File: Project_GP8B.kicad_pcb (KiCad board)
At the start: 4 copper layers, 133 x 93 mm, 103 parts, among them IC1 XC2C256-VQ100, J1 ALU_JTAG, J2 TE_Eurocard_96pole, J3 MM1_5530843-2, J4 UnusedPins_Connector, J5 ALU_PINS, U1 74AHC05, U10 74AHC1G04, U11 CD74AC238, U12 74AHC1G04, U13 CD74AC238, U14 74AHC08, U15 CD74AC238, U16 74AHC08, U17 74AHC138, U18 74HC165, U19 74AHCT244, U2 74AHC05, U20 74AHCT244, U21 74AHCT244, U22 74AHCT244, U23 74AHCT244, U24 74AHC273, U25 74AHCT595, U26 74AHC273, U27 74AHC273, U28 TPS7A0518PDBZR, U29 74AHC273, U3 74AHC1G04, U30 SN74LVC8T245DW, U31 74AHC273, U32 SN74AVC4T245D, U33 74AHC273, U34 74LVC1G34, U35 74AHC273, U36 74AHC1G04, U37 74AHC273, U38 74AHC374, U39 74AHC1G04, U4 74AHC1G04, U5 74AHC05, U6 74AHC273, U7 74AHCT273, U8 74HC163, U9 CD74AC238

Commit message: Apply date (19.08.2020), QRcode fix
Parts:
- added G***: LOGO, QRCode:QRCode, B.Cu at (157.3, 80.8)

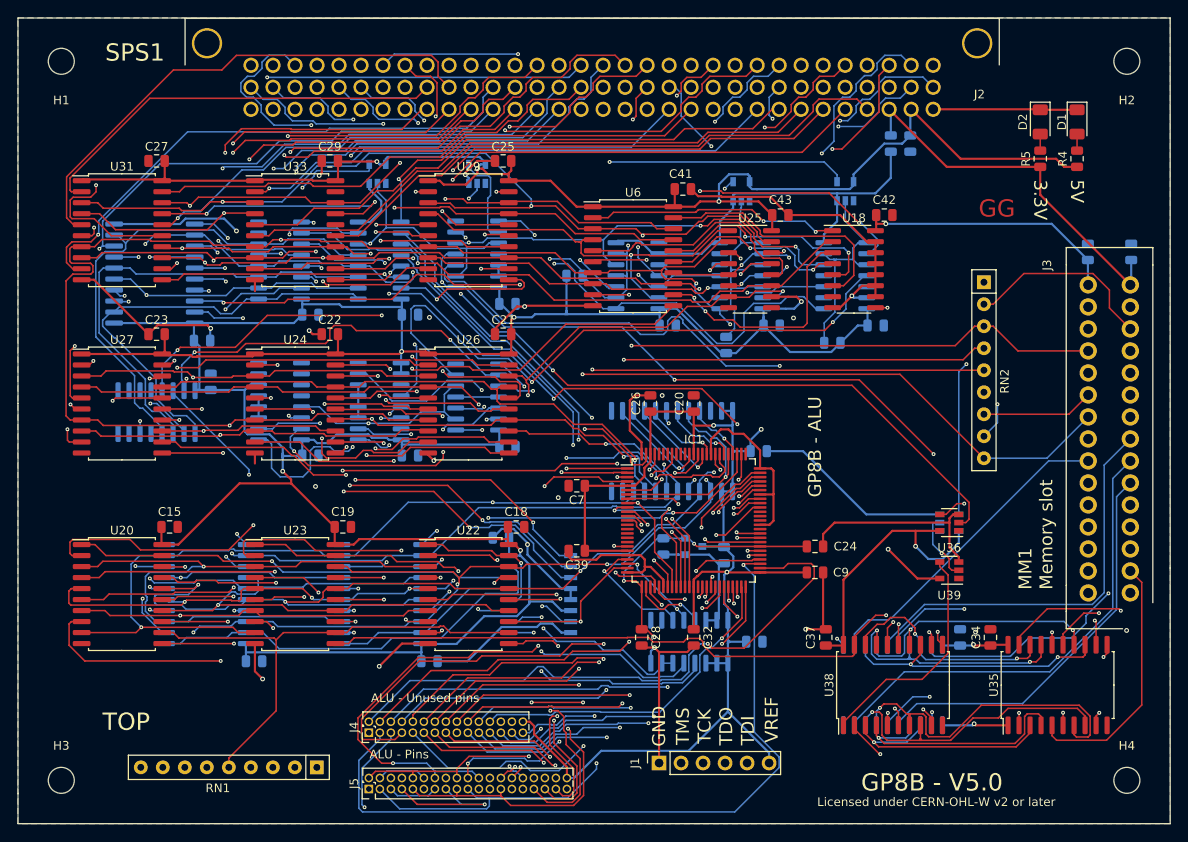
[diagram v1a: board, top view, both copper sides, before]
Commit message: V5.1 (#9)
* Apply new symbol for XC2C256-VQ100 #5

* Set new date and 5.1

* Replacing 74HC165 with 74HC166, and add SPI_CFG_DS #4

* Replace some gates with a 74AHC1G02 to fix the pulse problem #3

* Go next only if SRCVALUE, (simple instruction)

* Remove weird ghost bus in register

* Small cleaning in fileRegister

* Go next only if SRCVALUE, (complex instruction) #8
adding 74AHC1G08

* Better decoupling #6

* Component association (#7)

* netlist

* Updated BOM for V5.1

* Routing, cleaning first pass

* bit of pcb cleaning

* SolderMaskClearance to 0

* Schematics to pdf

* PCB files in pdf

* exporting Gerbert files

* new 3d images

* Update README.md

* Modifying CHANGELOG file

* Update README.md
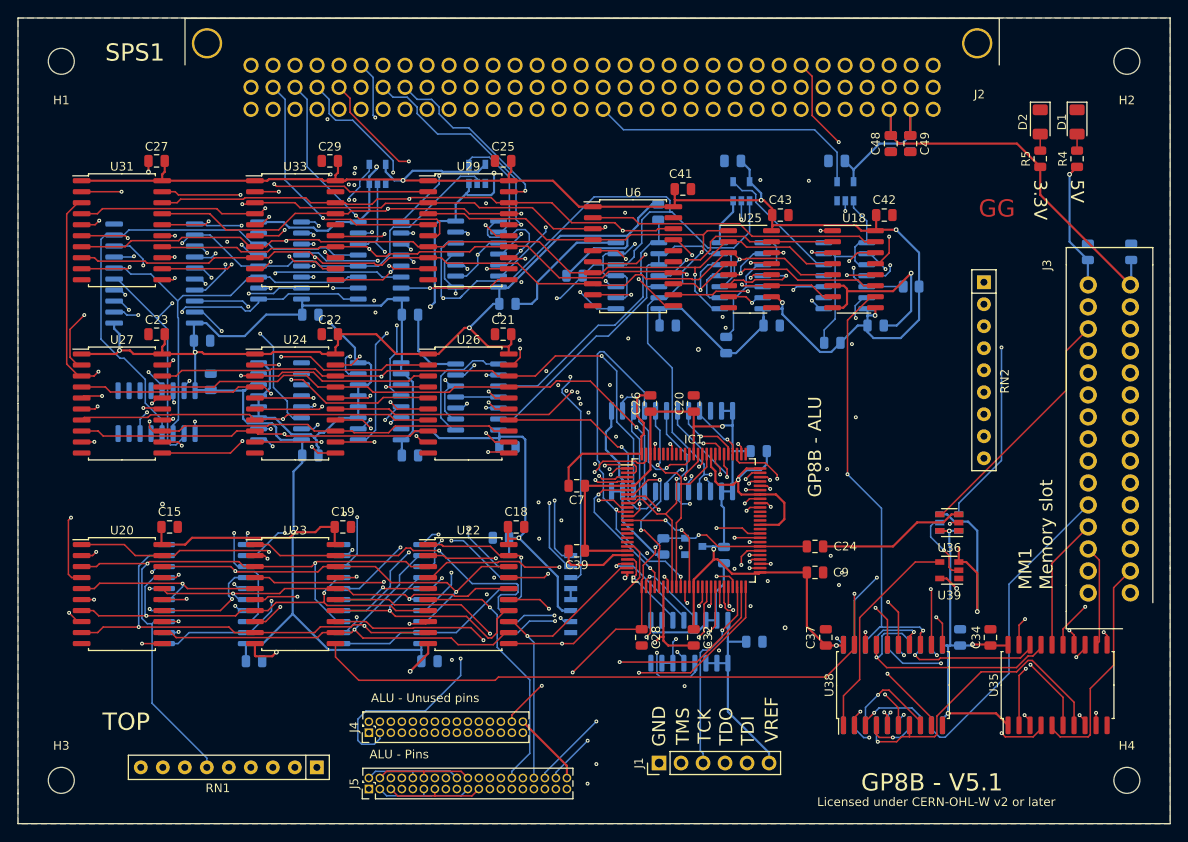
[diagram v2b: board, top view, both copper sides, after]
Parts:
- added C46: 10nF, Capacitor_SMD:C_0805_2012Metric, B.Cu at (155.5, 48.0)
- added C47: 10nF, Capacitor_SMD:C_0805_2012Metric, B.Cu at (143.5, 48.0)
- added C48: 1uF, Capacitor_SMD:C_0805_2012Metric, F.Cu at (161.8, 46.0)
- added C49: 1uF, Capacitor_SMD:C_0805_2012Metric, F.Cu at (164.0, 46.0)
- added R6: 10k, Resistor_SMD:R_0805_2012Metric, B.Cu at (134.9, 53.9)
- added R7: 10k, Resistor_SMD:R_0805_2012Metric, B.Cu at (164.1, 62.5)
- C30, C31, C36, C38: value 10nF -> 100nF
- J1: footprint Connector_PinSocket_2.54mm:PinSocket_1x06_P2.54mm_Vertical -> Connector_PinHeader_2.54mm:PinHeader_1x06_P2.54mm_Vertical
- U18: value 74HC165 -> 74HC166
- U3: value 74AHC1G04 -> 74AHC1G02
- U4: value 74AHC1G04 -> 74AHC1G08
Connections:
- R3 pad 2: /~ADDSRC_CLK -> /~NEXT_CLK
- U1 pad 8: Net-(U1-Pad8) -> /IF_RESULT
- U1 pad 9: GND -> /~IF_RESULT
- U14 pad 11: Net-(U14-Pad11) -> /NEXT_ISIMPLE
- U14 pad 12: GND -> /END_ISIMPLE
- U14 pad 13: GND -> /SELECTING_SRC
- U17 pad 15: /NumberSelect/~SELECTING_SRC -> /~SELECTING_SRC
- U18 pad 1: /SPI/SPI_CFG_~PL -> /SPI/SPI_CFG_DS
- U18 pad 10: GND -> /NUMBER_4
- U18 pad 11: GND -> /NUMBER_5
- U18 pad 12: GND -> /NUMBER_6
- U18 pad 13: GND -> /SPI_MOSI
- U18 pad 14: GND -> /NUMBER_7
- U18 pad 15: GND -> /SPI/SPI_CFG_~PL
- U18 pad 2: /SPI_CLK -> /NUMBER_0
- U18 pad 3: /SPI/BUFF_0 -> /NUMBER_1
- U18 pad 4: /SPI/BUFF_1 -> /NUMBER_2
- U18 pad 5: /SPI/BUFF_2 -> /NUMBER_3
- U18 pad 6: /SPI/BUFF_3 -> GND
- U18 pad 7: Net-(U18-Pad7) -> /SPI_CLK
- U18 pad 9: /SPI_MOSI -> +5V
- U19 pad 1: /NumberSelect/~SELECTING_SRC -> /~SELECTING_SRC
- U19 pad 19: /NumberSelect/~SELECTING_SRC -> /~SELECTING_SRC
- U3 pad 1: (no net) -> /~NEXT_CLK
- U3 pad 2: /~ADDSRC_CLK -> /GLOBAL_CLK
- U4 pad 1: (no net) -> /END_MAXCOUNT
- U4 pad 2: /~IF_RESULT -> /SELECTING_SRC
- U4 pad 4: /IF_RESULT -> /NEXT_MAXCOUNT
- U5 pad 1: /END_ISIMPLE -> /NEXT_ISIMPLE
- U5 pad 10: /~ADDSRC_CLK -> /~NEXT_CLK
- U5 pad 12: Net-(U5-Pad12) -> /SELECTING_SRC
- U5 pad 13: GND -> /~SELECTING_SRC
- U5 pad 2: /~ADDSRC_CLK -> /~NEXT_CLK
- U5 pad 4: /~ADDSRC_CLK -> /~NEXT_CLK
- U5 pad 5: /END_MAXCOUNT -> /NEXT_MAXCOUNT
- U5 pad 6: /~ADDSRC_CLK -> /~NEXT_CLK
- U5 pad 8: /~ADDSRC_CLK -> /~NEXT_CLK
- U6 pad 12: /SPI/BUFF_0 -> /SPI_CS
- U6 pad 15: /SPI/BUFF_1 -> Net-(U6-Pad15)
- U6 pad 16: /SPI/BUFF_2 -> Net-(U6-Pad16)
- U6 pad 19: /SPI/BUFF_3 -> Net-(U6-Pad19)
- U6 pad 6: /SPI_SCLK -> /SPI/SPI_CFG_DS
- U6 pad 9: /SPI_CS -> /SPI_SCLK
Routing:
- net /~SELECTING_SRC: track 0.00 -> 108.1 mm, vias 0 -> 3
- net GND: track 420.0 -> 338.7 mm, vias 20 -> 17
- net /BRAMADD1_CLK: track 184.9 -> 120.4 mm, vias 2 -> 3
- net /SELECTING_SRC: track 0.00 -> 56.4 mm, vias 0 -> 3
- net /Connector/BREAD1_7: track 99.3 -> 147.9 mm
- net /NumberSelect/~SELECTING_SRC: track 48.3 -> 0.00 mm
- net /NUMBER_1: track 434.3 -> 391.3 mm, vias 8 -> 10
- net /NEXT_ISIMPLE: track 0.00 -> 42.2 mm, vias 0 -> 2
- net /NUMBER_7: track 407.7 -> 369.6 mm, vias 12 -> 11
- net /PROCESSOR_PAUSE: track 70.3 -> 103.4 mm, vias 2 -> 1
- net /NUMBER_2: track 386.9 -> 419.8 mm
- net /SPI_MOSI: track 60.8 -> 28.0 mm, vias 1 -> 2
- net /GLOBAL_CLK: track 54.1 -> 86.9 mm, vias 1 -> 4
- net /NUMBER_3: track 423.6 -> 392.0 mm
- net /Connector/BWRITE2_5: track 82.3 -> 50.8 mm
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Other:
- rule pad_to_mask_clearance: 0.2 -> 0
- board text added: "GP8B - V5.1"
- board text removed: "GP8B - V5.0"

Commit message: Transition to kicad version 6
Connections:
- net /Instruction/~COUNTER_2 renamed /Instruction/~{COUNTER_2}
- net /Instruction/~INSTRUCTION_B5 renamed /Instruction/~{INSTRUCTION_B5}
- net /NumberSelect/~SELECTING_BREAD1 renamed /NumberSelect/~{SELECTING_BREAD1}
- net /NumberSelect/~SELECTING_BREAD2 renamed /NumberSelect/~{SELECTING_BREAD2}
- net /NumberSelect/~SELECTING_OPRESULT renamed /NumberSelect/~{SELECTING_OPRESULT}
- net /NumberSelect/~SELECTING_RAM renamed /NumberSelect/~{SELECTING_RAM}
- net /RAM/B_RAM_~OE renamed /RAM/B_RAM_~{OE}
- net /RAM/RAM_~WE renamed /RAM/RAM_~{WE}
- net /SPI/SPI_CFG_~PL renamed /SPI/SPI_CFG_~{PL}
- net /~COUNTER_RESET renamed /~{COUNTER_RESET}
- net /~IF_RESULT renamed /~{IF_RESULT}
- net /~NEXT_CLK renamed /~{NEXT_CLK}
- net /~SELECTING_RBEXT1 renamed /~{SELECTING_RBEXT1}
- net /~SELECTING_RBEXT2 renamed /~{SELECTING_RBEXT2}
- net /~SELECTING_SPI renamed /~{SELECTING_SPI}
- net /~SELECTING_SRC renamed /~{SELECTING_SRC}
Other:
- net class Default removed
- net class Volt removed
